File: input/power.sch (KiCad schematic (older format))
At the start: 30 parts, among them Q2 2STD1665T4, Q3 NSS1C300ET4G, U4 OPA830, U6 OPA830

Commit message: Mostly work on power, regulators and distribution.  Also more BOM cleanup.
All of the bypass capacitors are now spec'd and in the DigiKey BOM. TVS zeners are now
spec'd.  Folded together some resistor values and got rid of some 1206 parts that no longer
need that much power rating at the lower supplies.

A affecting all of the input channel sheets is that we now distribute filtered V+, V- and VREF
via sheet ports.  The V+, V- filter is on input_channel.sch and the VREF filter is still in
adc.sch, but is distributed out to the other sheets that need it.

bist_buffer.sch: added buffer for built-in self-test

board_connector.sch: put the input filter for the analog supplies here.

power.sch: added regulators for the supplies.

reference_buffer.sch:
changed components to match those chosen for the V+, V- regulators and added
current steering diodes to bootstrap the reference buffer supply.  This is
necessary because the analog supplies are now derived from VREF.

*.wxsch:
Updates to spice models related to work on supplies.
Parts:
- added C22, C23: 1uF, Capacitor_SMD:C_0805_2012Metric, symbol Device:C_Small
- added C24: 10uF, Capacitor_SMD:C_0603_1608Metric, symbol Device:C_Small
- added C25, C26: 330uF, Capacitor_SMD:CP_Elec_8x6.7, symbol Device:CP1_Small
- added D10, D11: 5V (standoff), Diode_SMD:D_SMA, symbol Device:D_Zener
- added FB3, FB4: 21 Ohm, digikey-footprints:0805, symbol dk_Ferrite-Beads-and-Chips:MPZ2012S601AT000
- added R21, R22: 200, Resistor_SMD:R_0603_1608Metric, symbol Device:R_US
- added U7: MCP1755S-3302E/DB, Package_TO_SOT_SMD:SOT-223-3_TabPin2, symbol Regulator_Linear:MCP1703A-1202_SOT223
- added U8: NCP1117STAT3G, Package_TO_SOT_SMD:SOT-223, symbol dk_PMIC-Voltage-Regulators-Linear:NCP1117ST33T3G
- C10, C8, C9: footprint Capacitor_SMD:C_0603_1608Metric -> Capacitor_SMD:C_0805_2012Metric; Description (none) -> CAP CER 1UF 16V X7R 0805; Digikey (none) -> 1276-6471-1-ND; MPN (none) -> CL21B105KOFNNNG
- C11, C14, C15, C7: Description (none) -> 16V aluminum solid polymer, ESR 22 mOhm; Digikey (none) -> 565-4285-1-ND; MPN (none) -> APXG160ARA331MH70G
- C12, C13: value 150pF -> 47pF; footprint Capacitor_SMD:C_0805_2012Metric -> Capacitor_SMD:C_0603_1608Metric; Description CAP CER 10000PF 50V C0G/NP0 0805 -> (none); Digikey 490-8296-1-ND -> (none); MPN GRM2195C1H103GA01D -> (none); Notes 2% C0G -> (none)
- R10, R11, R13, R8: Description (none) -> RES SMD 499 OHM 0.1% 1/4W 0805; Digikey (none) -> A110514CT-ND
- R14: footprint Resistor_SMD:R_1206_3216Metric -> Resistor_SMD:R_0603_1608Metric; Notes (none) -> 0.1%
- R15, R16: footprint Resistor_SMD:R_1206_3216Metric -> Resistor_SMD:R_0805_2012Metric; Digikey (none) -> 541-10TACT-ND; Notes (none) -> Thick film surge resist
- R17, R18: footprint Resistor_SMD:R_1206_3216Metric -> Resistor_SMD:R_0603_1608Metric
- gave numbers to parts that had none: 1
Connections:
- net GNDA: now also C23.1, C24.2, C26.2, D11.2 (A), R22.1
- new net: C24.1, R21.1, R22.2, U8.1 (ADJ/GND)
- new net: C23.2, D11.1 (K), FB4.2, U8.3 (IN)
- new net: C22.2, D10.1 (K), FB3.2, U7.1 (VI)
- new net GNDD: C22.1, C25.2, D10.2 (A), U7.2 (GND)
- new net OVDD: C25.1, U7.3 (VO)
- new net RAW_+5VANA: FB4.1
- new net RAW_+5VDIG: FB3.1
- new net VDD: C26.1, R21.2, U8.2 (OUT), U8.4 (OUT)
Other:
- note added: "+2.5V ADC supply"
- note added: "+3.3V digital"
- moved on the sheet: C10, C11, C12, C14, C15, C7, C8, C9, D3A, D3B, F1, F2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

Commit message: Mostly finished wiring.
Finished mapping pins in board_connector.sch.  Renamed some nets and moved the analog
supply filter to power.sch.  Added probe_connector.sch which now includes input protected
on the probe calibration one-wire line.  The configuration digital interface stuff is still
sketchy, this is basically a placeholder.  Eventually we will have an I2C I/O extender for
configuration and calibration memory, but for now I added a jumper header for setting the
SEL0/SEL1 lines to control the ADC decimation.
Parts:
- added C16, C17, C18, C19: 1uF, Capacitor_SMD:C_0805_2012Metric, symbol Device:C_Small
- added C20, C21: 330uF, Capacitor_SMD:CP_Elec_8x6.7, symbol Device:CP1_Small
- added D4, D8: 10V (standoff), Diode_SMD:D_SMA, symbol Device:D_Zener
- added FB1, FB2: 21 Ohm, digikey-footprints:0805, symbol dk_Ferrite-Beads-and-Chips:MPZ2012S601AT000
- added FL1: 100uH, input:L_CommonMode_Wuerth_WE-SL3, symbol ilemt_input:EMI_Filter_CommonMode_3Line
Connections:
- net GNDA: now also C16.1, C17.2, C18.1, C19.2, C20.2, C21.1, D4.2 (A), D8.1 (K), FL1.5
- net RAW_V+ renamed FILT_+10V
- net FILT_+10V: now also C18.2, C20.1, FB2.2
- net RAW_V- renamed FILT_-6V
- net FILT_-6V: now also C19.1, C21.2, FB1.2
- new net: C17.1, D8.2 (A), FB1.1, FL1.4
- new net: C16.2, D4.1 (K), FB2.1, FL1.6
- new net +10V_-6V_RETURN: FL1.2
- new net RAW_+10V: FL1.1
- new net RAW_-6V: FL1.3
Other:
- moved on the sheet: C10, C11, C12, C13, C14, C15, C22, C23, C24, C25, C26, C7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

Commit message: Cleanup to get ready to start board layout. I had to get rid off all the bus signals, since in Kicad busses don't work that way.  Added a couple testpoints; many more needed.
Work on component placement in PCB.  I changed DGND to plain GND and "protective earth" to
"earth" (for chassis ground).  Chassis ground is now connected on the board only via a capacitor.
I had to fix the connector footprint to match the pin numbers on the symbol (there was a case
difference).
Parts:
- removed unit 1 of D3
- added C32: 10nF, Capacitor_SMD:C_0805_2012Metric, symbol Device:C_Small
- added unit 1 of D3
- D3: symbol Diode:BAV99 -> ilemt_input:BAS21S
- FB1, FB2, FB3, FB4: footprint digikey-footprints:0805 -> Inductor_SMD:L_0805_2012Metric
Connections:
- net GNDD is gone; now on net GND: C22.1, C25.2, D10.2 (A), U7.2 (GND)
- net RAW_+10V: now also FL1.3; no longer FL1.1
- net RAW_-6V: now also FL1.1; no longer FL1.3
- net at C9.2, R14.2, U6.7 (V+): now also D3.1 (A)
- net at D3.3 (A): now also D3.3 (K)
- net at C17.1, D8.2 (A), FB1.1: now also FL1.6; no longer FL1.4
- net at C16.2, D4.1 (K), FB2.1: now also FL1.4; no longer FL1.6
- net GNDA renamed GND
- net GND: now also C32.2
- new net Earth: C32.1
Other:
- moved on the sheet: C26

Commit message: Progress on input board layout.  Have adopted 100x280mm eurocard format with connector at the back. Schematic changes are mostly cosmetic.  The working board file is now input/input_board_rear.kicad_pcb
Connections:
- net GND: now also C11.1, C15.1; no longer C11.2, C15.2
- net V-: now also C15.2; no longer C15.1
- net at C10.2, R16.1, U6.4 (V-): now also C11.2; no longer C11.1
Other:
- note added: "R15/C7 and R16/C11 boost the 10 kHz supply rejection\nabove the U5, U6 PSRR (which will be low in a high speed type)"
- note added: "These regulators for the V+, V- analog supplies operate at a lowish dropout of about 1.5V\nand clean up any crud on the incoming supplies. They also give a supply referenced\nto the local ground which is extremely stiff at our operating frequency near 10 kHz.\nThis prevents coupling between channels via the supply. \n\nThe outputs are derived from the VREF 5V reference, which has to be low noise,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"
- note removed: "V+, V- are the analog supplies. They operate at a lowish dropout of about 1.5V\nand clean up any crud on the incoming supplies. They also give a supply referenced\nto the local ground which is extremely stiff at our operating frequency near 10 kHz.\nThis prevents coupling between channels via the supply.\n\nBecause the PSRR of the stage 1 amp is only 60 dB at 10 kHz, and the PSRR effect \nshould 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"
- moved on the sheet: C10, C11, C12, C13, C14, C15, C16, C17, C18, C19, C20, C21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

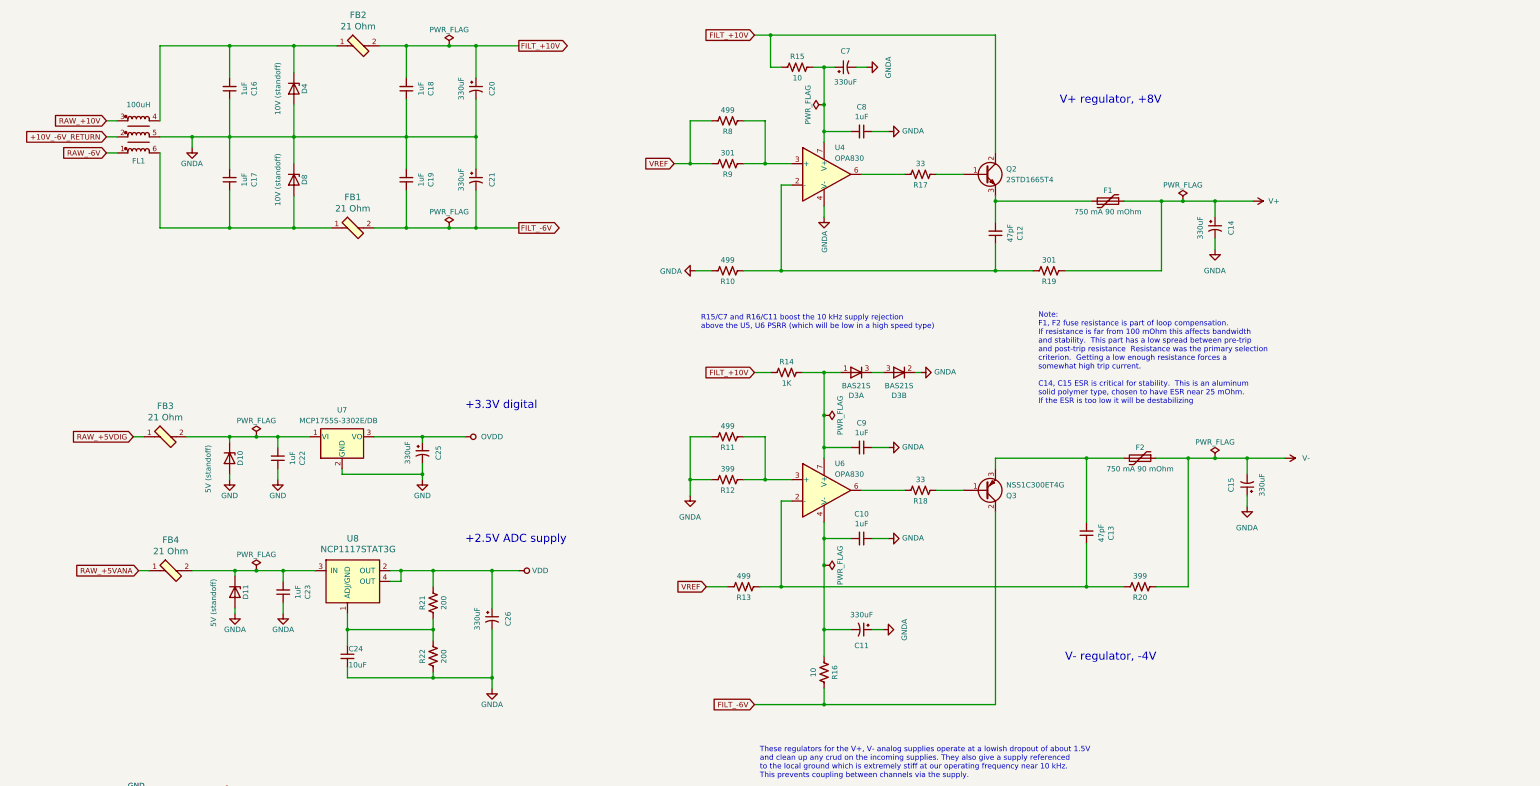
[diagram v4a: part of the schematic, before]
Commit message: Changed board connector to PCIe 8x, added test points, cleanup of component values. Add LVDS Rx termination, bypass caps.
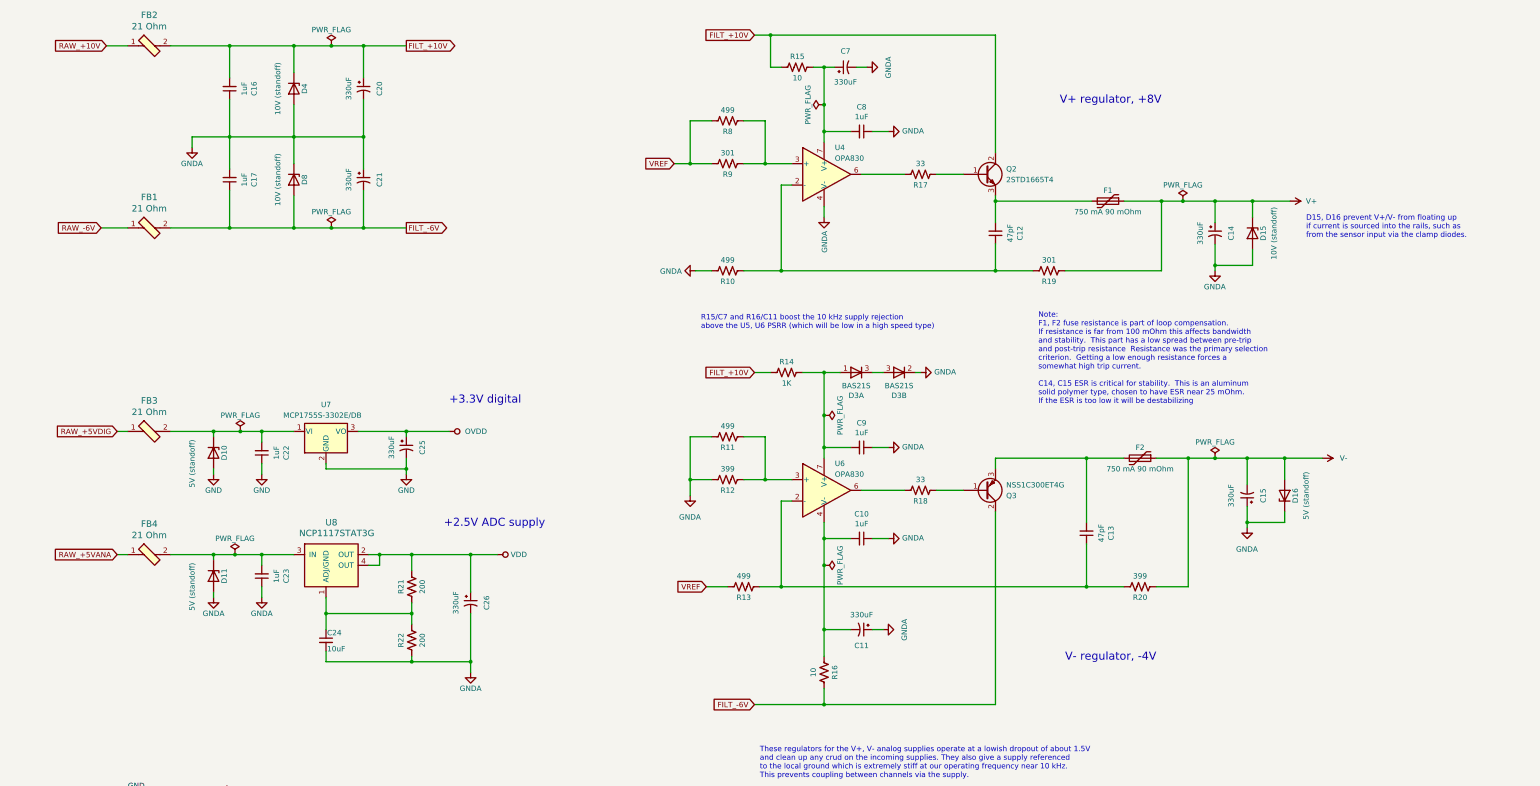
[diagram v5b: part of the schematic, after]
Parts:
- removed C18, C19: 1uF, Capacitor_SMD:C_0805_2012Metric, symbol Device:C_Small
- removed FL1: 100uH, input:L_CommonMode_Wuerth_WE-SL3, symbol ilemt_input:EMI_Filter_CommonMode_3Line
- added D15: 10V (standoff), Diode_SMD:D_SMA, symbol Device:D_Zener
- added D16: 5V (standoff), Diode_SMD:D_SMA, symbol Device:D_Zener
- R12, R20: footprint Resistor_SMD:R_0805_2012Metric -> Resistor_SMD:R_0603_1608Metric
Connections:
- net FILT_+10V: now also C16.2, D4.1 (K)
- net FILT_-6V: now also C17.1, D8.2 (A)
- net GND: now also D15.2 (A), D16.1 (K)
- net RAW_+10V: now also FB2.1
- net RAW_-6V: now also FB1.1
- net V+: now also D15.1 (K)
- net V-: now also D16.2 (A)
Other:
- note added: "D15, D16 prevent V+/V- from floating up\nif current is sourced into the rails, such as\nfrom the sensor input via the clamp diodes."
- moved on the sheet: C14, C15, C20, C21, C22, C23, C24, C25, C26, D10, D11, FB1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

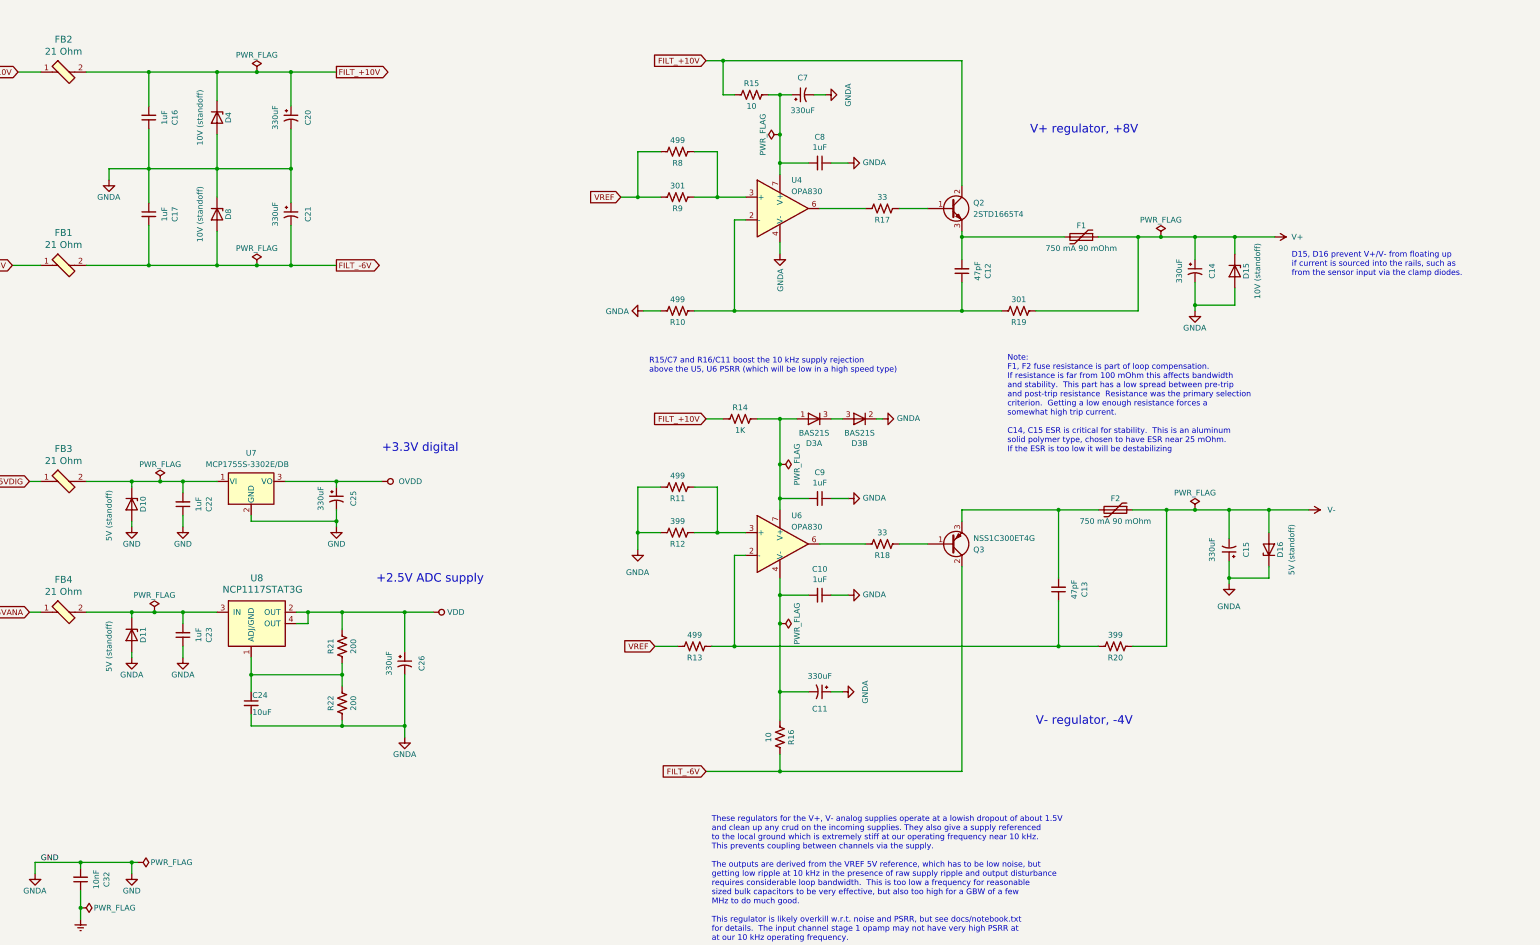
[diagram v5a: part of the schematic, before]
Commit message: Checkpoint before starting routing.  Added power and ground testpoints.
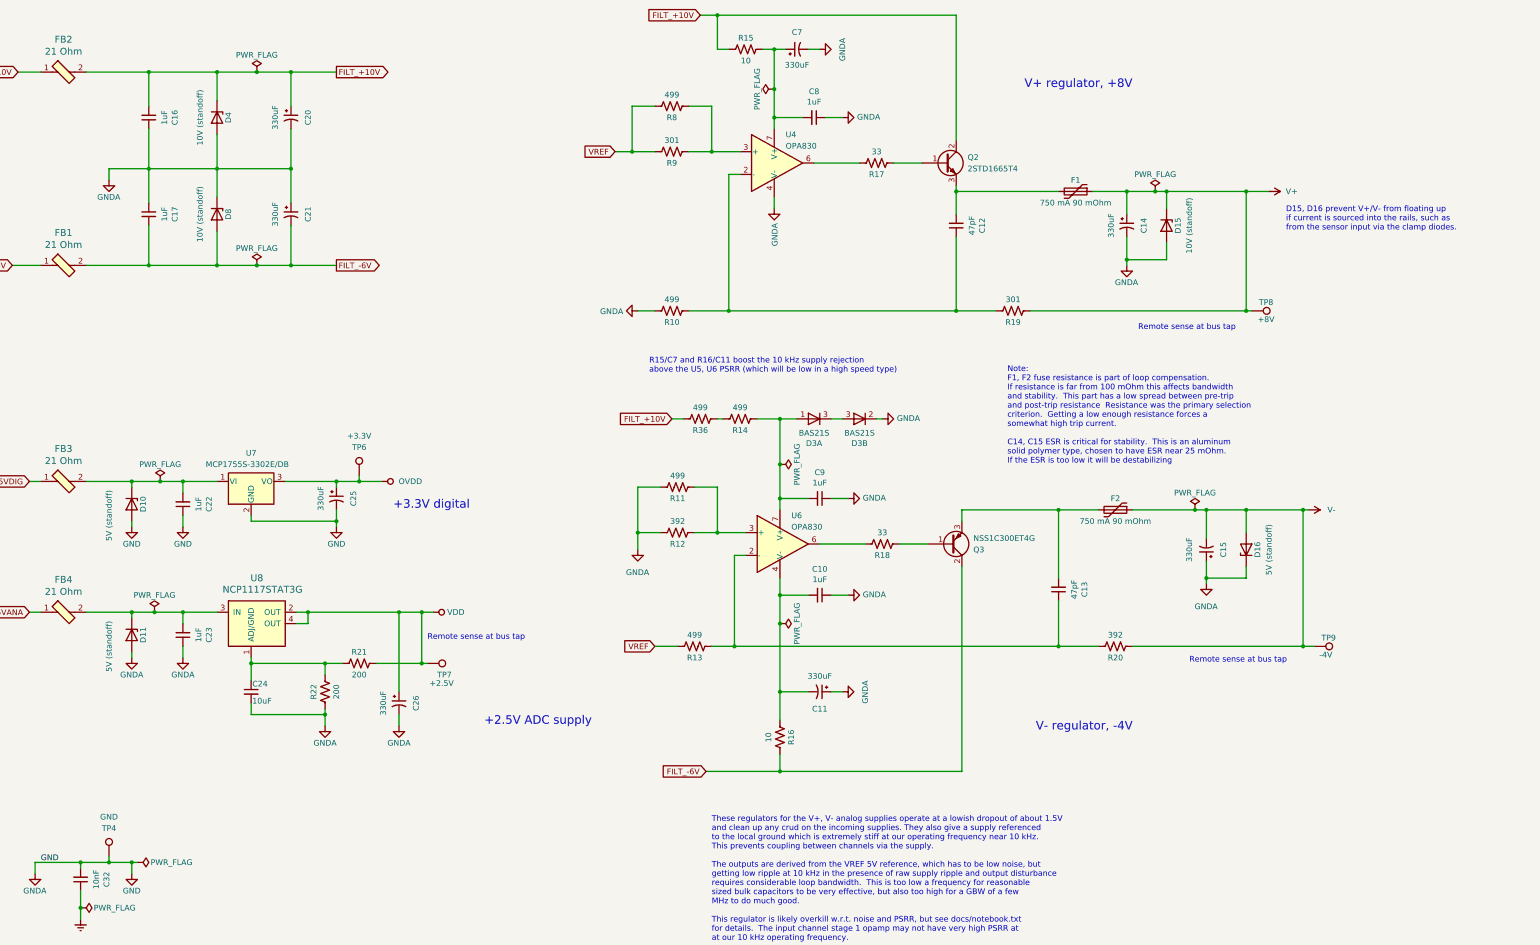
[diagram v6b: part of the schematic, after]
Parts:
- added R36: 499, Resistor_SMD:R_0805_2012Metric, symbol Device:R_US
- added TP4: GND, input:TestPoint_THTPad_D5.0mm_Drill2.41mm, symbol Connector:TestPoint
- added TP6: +3.3V, TestPoint:TestPoint_THTPad_D1.5mm_Drill0.7mm, symbol Connector:TestPoint
- added TP7: +2.5V, TestPoint:TestPoint_THTPad_D1.5mm_Drill0.7mm, symbol Connector:TestPoint
- added TP8: +8V, TestPoint:TestPoint_THTPad_D1.5mm_Drill0.7mm, symbol Connector:TestPoint
- added TP9: -4V, TestPoint:TestPoint_THTPad_D1.5mm_Drill0.7mm, symbol Connector:TestPoint
- C10, C16, C17, C22, C23, C8, C9: DK line (none) -> 27
- C11, C14, C15, C20, C21, C25, C26, C7: DK line (none) -> 19
- C12, C13: DK line (none) -> 44; Description (none) -> 47pF ±5% 50V Ceramic Capacitor C0G, NP0 0603 (1608 Metric); Digikey (none) -> 311-1065-1-ND
- C24: DK line (none) -> 29
- C32: DK line (none) -> 14
- D10, D11, D16: DK line (none) -> 40
- D15, D4, D8: DK line (none) -> 41; Description TVS DIODE 5V 9.2V DO214AC -> TVS DIODE 10V 17V DO214AC; Digikey 732-9974-1-ND -> 732-9947-1-ND
- D3: DK line (none) -> 43; Description (none) -> DIODE ARRAY GP 250V 225MA SOT23; Digikey (none) -> BAS21SLT1GOSCT-ND; MPN (none) -> BAS21SLT1G
- F1, F2: DK line (none) -> 21; Description (none) -> PTC RESET FUSE 16V 750MA 1206; Digikey (none) -> 507-1805-1-ND
- FB1, FB2, FB3, FB4: DK line (none) -> 24
- Q2: DK line (none) -> 22
- Q3: DK line (none) -> 23
- R10, R11, R13, R8: DK line (none) -> 30
- R12, R20: value 399 -> 392; DK line (none) -> 49; Description (none) -> 392 Ohms ±1% 0.125W, 1/8W Chip Resistor 0603 (1608 Metric) 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; Digikey (none) -> RNCP0603FTD392RCT-ND
- R14: value 1K -> 499; footprint Resistor_SMD:R_0603_1608Metric -> Resistor_SMD:R_0805_2012Metric; DK line (none) -> 30; Description (none) -> RES SMD 499 OHM 0.1% 1/4W 0805; Digikey (none) -> A110514CT-ND
- R15, R16: DK line (none) -> 9; Description (none) -> RES SMD 10 OHM 5% 1/2W 0805; MPN (none) -> CRCW080510R0JNEAHP
- R17, R18: DK line (none) -> 52; Digikey (none) -> RMCF0603FT33R0CT-ND
- R19, R9: DK line (none) -> 50; Description (none) -> 301 Ohms ±1% 0.125W, 1/8W Chip Resistor 0603 (1608 Metric) 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; Digikey (none) -> RNCP0603FTD301RCT-ND
- R21, R22: DK line (none) -> 55; Description (none) -> 200 Ohms ±1% 0.125W, 1/8W Chip Resistor 0603 (1608 Metric) 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; Digikey (none) -> RNCP0603FTD200RCT-ND
- U4, U6: DK line (none) -> 20; Description (none) -> IC OPAMP VFB 1 CIRCUIT 8SOIC; Digikey (none) -> 296-17400-5-ND
- U7: DK line (none) -> 25
- U8: DK line (none) -> 26
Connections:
- net FILT_+10V: now also R36.2; no longer R14.1
- net GND: now also TP4.1
- net OVDD: now also TP6.1
- net V+: now also TP8.1
- net V-: now also TP9.1
- net VDD: now also TP7.1
- net at C9.2, D3.1 (A), U6.7 (V+): now also R14.1; no longer R14.2
- new net: R14.2, R36.1
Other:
- note added: "Remote sense at bus tap"
- moved on the sheet: C12, C14, C15, C24, C26, C7, C8, D15, D16, F1, Q2, R10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
